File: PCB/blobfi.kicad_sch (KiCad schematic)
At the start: 9 parts, among them SW1 SW_Push, SW2 SW_Push, SW3 SW_Push, U1 XIAO-ESP32-C6-DIP, U2 HS96L03W2C03

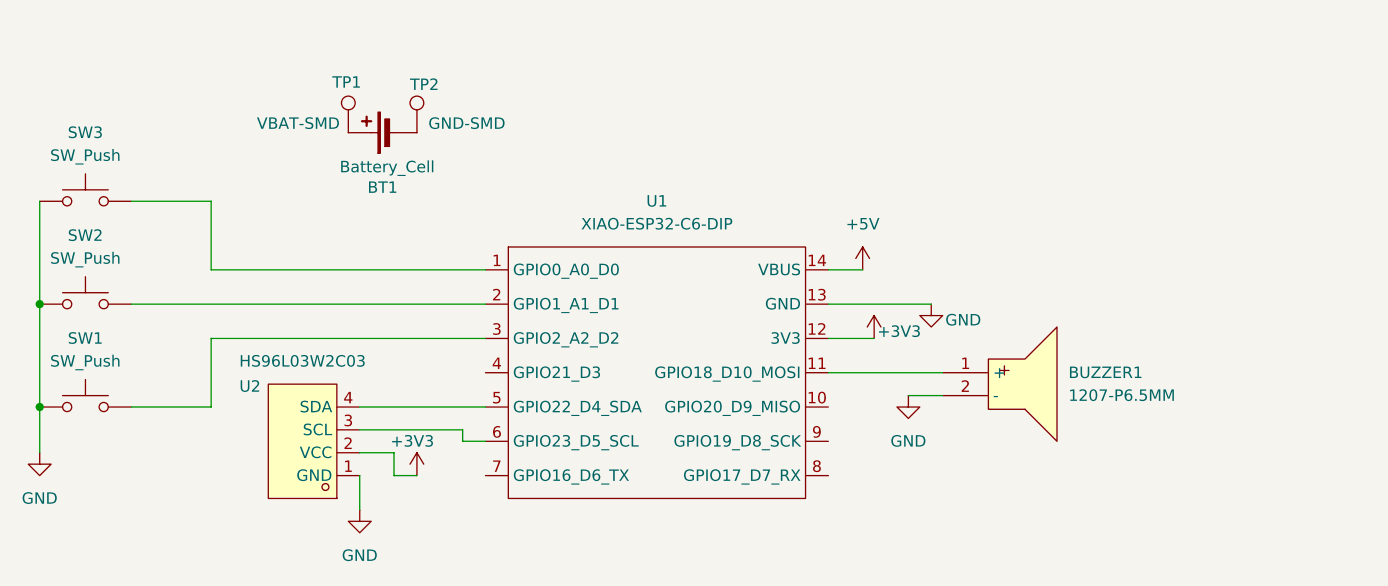
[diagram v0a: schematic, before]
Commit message: add proper warning
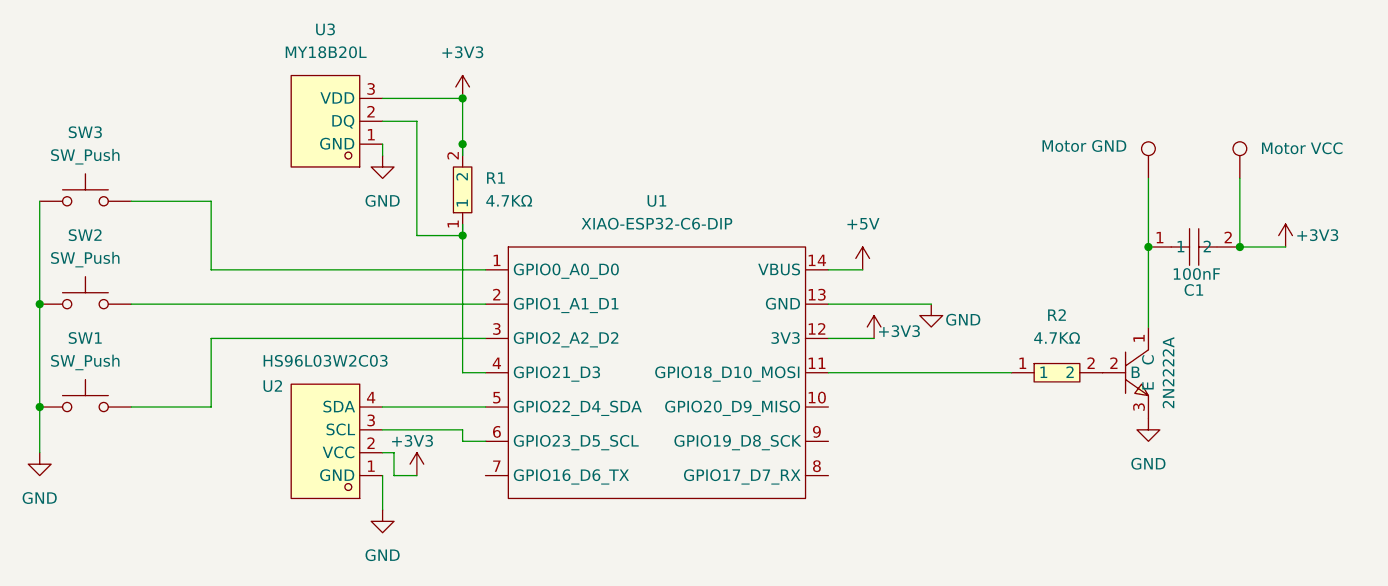
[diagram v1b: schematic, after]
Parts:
- removed BT1: Battery_Cell, Connector_PinHeader_2.54mm:PinHeader_1x02_P2.54mm_Vertical, symbol Device:Battery_Cell
- removed BUZZER1: 1207-P6.5MM, easyeda2kicad:BUZ-TH_BD12.5-P6.50-D1.4, symbol easyeda2kicad:1207-P6.5MM
- added C1: 100nF, easyeda2kicad:CAP-TH_L5.8-W3.6-P5.0-D0.6, symbol easyeda2kicad:178MU0003
- added Q1: 2N2222A, easyeda2kicad:TO-92-3_L4.8-W3.7-P2.54-R, symbol easyeda2kicad:2N2222A_C5330385
- added R1, R2: 4.7KΩ, easyeda2kicad:RES-TH_BD2.3-L6.5-P10.50-D0.5, symbol easyeda2kicad:MF1_4W-4.7KΩ±1%T52
- added U3: MY18B20L, easyeda2kicad:TO-92-3_L4.8-W3.7-P1.27-L, symbol easyeda2kicad:MY18B20L
- TP1: value VBAT-SMD -> Motor GND; footprint TestPoint:TestPoint_Pad_D2.0mm -> TestPoint:TestPoint_THTPad_1.5x1.5mm_Drill0.7mm
- TP2: value GND-SMD -> Motor VCC; footprint TestPoint:TestPoint_Pad_D2.0mm -> TestPoint:TestPoint_THTPad_1.5x1.5mm_Drill0.7mm
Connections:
- net +3V3: now also TP2.1, C1.2, R1.2, U3.3 (VDD)
- net GND: now also Q1.3 (E), U3.1 (GND)
- net at TP1.1: now also C1.1, Q1.1 (C)
- net at U1.11 (GPIO18_D10_MOSI): now also R2.1
- net at U1.4 (GPIO21_D3): now also R1.1, U3.2 (DQ)
- new net: Q1.2 (B), R2.2
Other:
- moved on the sheet: U2
